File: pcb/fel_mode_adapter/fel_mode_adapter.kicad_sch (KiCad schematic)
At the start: 4 parts, among them J1 USB_A, P1 USB_C_Plug_USB2.0

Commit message: Fix the board: add a regulator and farnelle references. Add a pull up on boot0
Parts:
- J1: farnell (none) -> 2313729
- P1: farnell (none) -> 3777659
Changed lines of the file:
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@@
+			)
+		)
+		(property "farnell" "2313729"
+			(at 175.26 85.09 0)
+			(effects
+				(font
+					(size 1.27 1.27)
+				)
+				(hide yes)
 			)
 		)
@@
 			(at 109.22 87.63 0)
 			(effects
+				(font
+					(size 1.27 1.27)
+				)
+				(hide yes)
+			)
+		)
+		(property "farnell" "3777659"
+			(at 109.22 87.63 0)
+			(effects

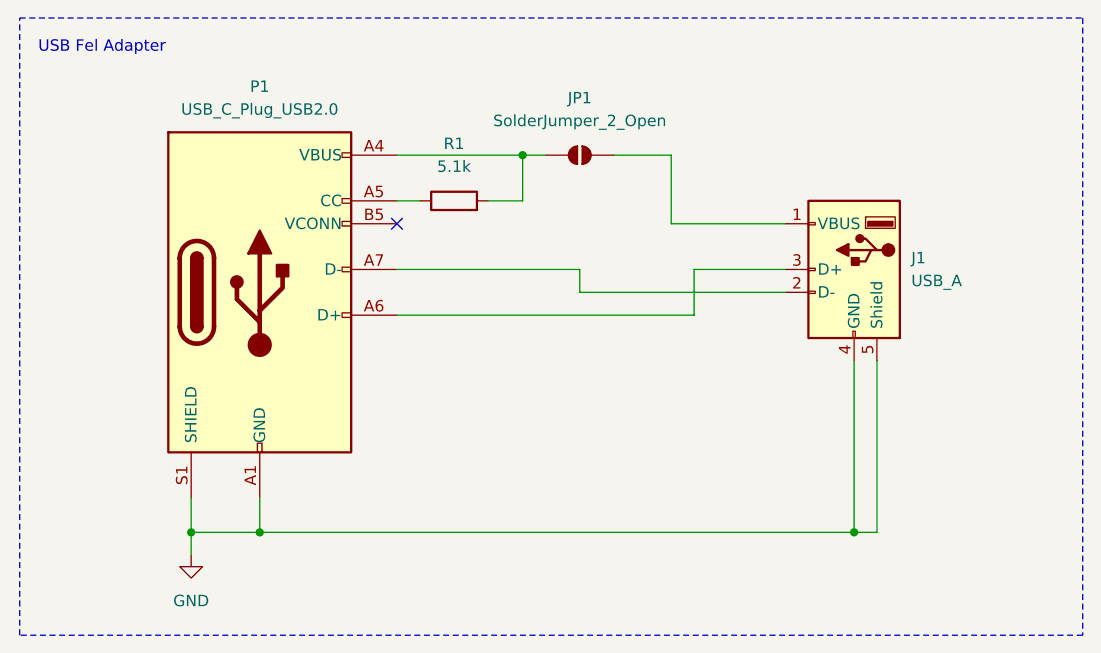
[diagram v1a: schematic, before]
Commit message: Adds a GND test point to the FEL mode adapter.
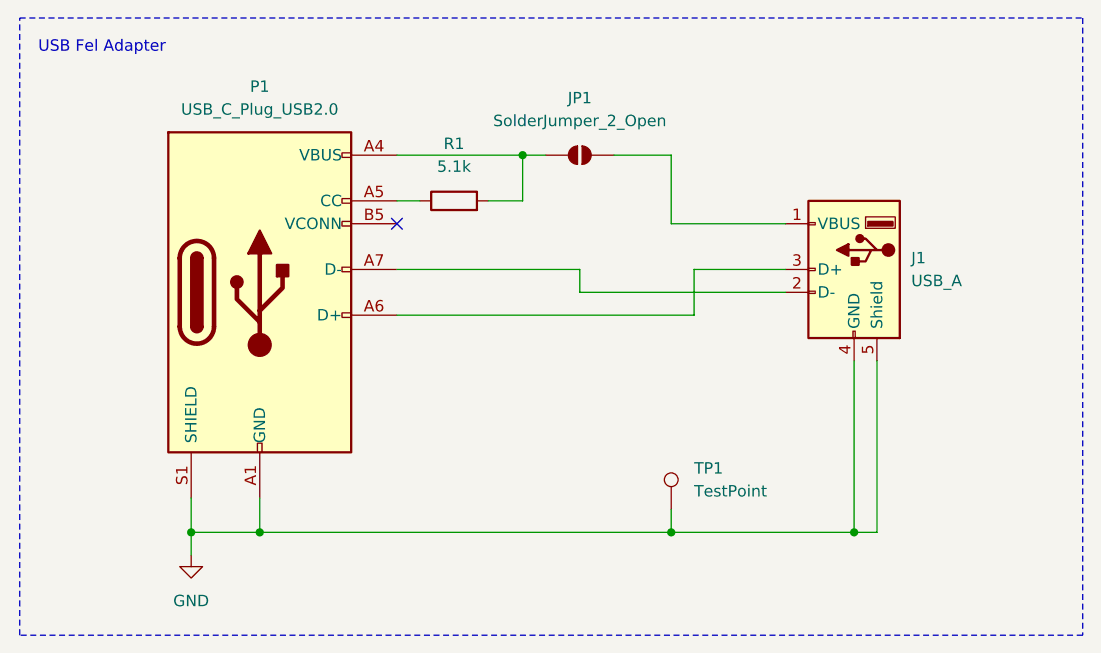
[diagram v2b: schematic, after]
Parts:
- added TP1: TestPoint, TestPoint:TestPoint_Pad_D1.0mm, symbol Connector:TestPoint
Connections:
- net GND: now also TP1.1
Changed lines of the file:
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@@
+		(color 0 0 0 0)
+	)
+	(junction
+		(at 154.94 114.3)
+		(diameter 0)
 		(color 0 0 0 0)
 	)
@@
 	(wire
 		(pts
+			(xy 154.94 114.3) (xy 109.22 114.3)
+		)
+		(stroke
+			(width 0)
+			(type default)
+		)
+	)
+	(wire
+		(pts
 			(xy 124.46 90.17) (xy 157.48 90.17)
 		)
@@
 	(wire
 		(pts
+			(xy 154.94 111.76) (xy 154.94 114.3)
+		)
+		(stroke
+			(width 0)
+			(type default)
+		)
+	)
+	(wire
+		(pts
 			(xy 177.8 114.3) (xy 175.26 114.3)
 		)
@@
 	(wire
 		(pts
-			(xy 175.26 114.3) (xy 109.22 114.3)
+			(xy 175.26 114.3) (xy 154.94 114.3)
 		)
 		(stroke
@@
 					(unit 1)
 				)
+			)
+		)
+	)
+	(symbol
+		(lib_id "Connector:TestPoint")
+		(at 154.94 111.76 0)
+		(unit 1)
+		(exclude_from_sim no)
+		(in_bom yes)
+		(on_board yes)
+		(dnp no)
+		(fields_autoplaced yes)
+		(property "Reference" "TP1"
+			(at 157.48 107.1879 0)
+			(effects
+				(font
+					(size 1.27 1.27)
+				)
+				(justify left)
+			)
+		)
+		(property "Value" "TestPoint"
+			(at 157.48 109.7279 0)
+			(effects
+				(font
+					(size 1.27 1.27)
+				)
+				(justify left)
+			)
+		)
+		(property "Footprint" "TestPoint:TestPoint_Pad_D1.0mm"
+			(at 160.02 111.76 0)
+			(effects
+				(font
+					(size 1.27 1.27)
+				)
+				(hide yes)
+			)
+		)
+		(property "Datasheet" "~"
+			(at 160.02 111.76 0)
+			(effects
+				(font
+					(size 1.27 1.27)
+				)
+				(hide yes)
+			)
+		)
+		(property "Description" "test point"
+			(at 154.94 111.76 0)
+			(effects
+				(font
+					(size 1.27 1.27)
+				)
+				(hide yes)
+			)
+		)
+		(pin "1"
+		)
+		(instances
+			(project ""
+				(path "/1418d05e-d255-4e21-84d2-420121b241e4"
+					(reference "TP1")
+					(unit 1)
+				)

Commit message: Updating the uart and fel mode adapter after soldering it.
Manufacturing shiwed the pcb to be too large and the gnd wire connector
too close to the uart connector. The farnell reference resistor on the
fel mode adapter was of the wrong foorprint.
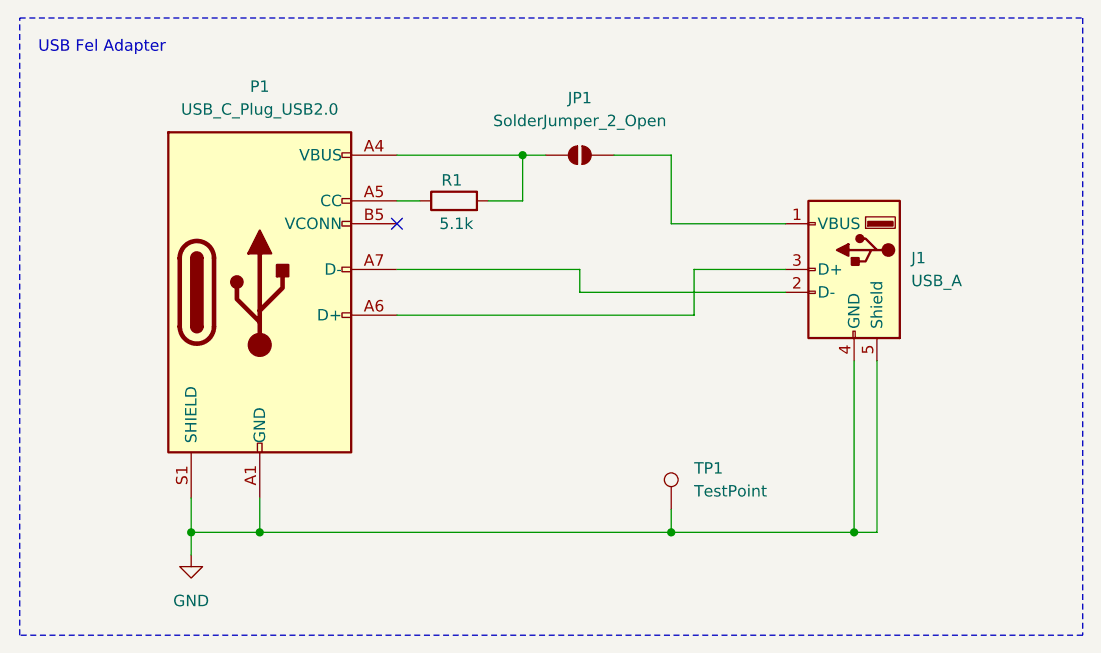
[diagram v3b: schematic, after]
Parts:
- R1: farnell (none) -> 9334645
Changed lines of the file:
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@@
 		(on_board yes)
 		(dnp no)
-		(fields_autoplaced yes)
 		(property "Reference" "R1"
-			(at 130.81 71.12 90)
+			(at 130.556 75.184 90)
 			(effects
 				(font
@@
 		)
 		(property "Value" "5.1k"
-			(at 130.81 73.66 90)
+			(at 131.064 80.01 90)
 			(effects
 				(font
@@
 			(at 130.81 77.47 0)
 			(effects
+				(font
+					(size 1.27 1.27)
+				)
+				(hide yes)
+			)
+		)
+		(property "farnell" "9334645"
+			(at 130.81 77.47 0)
+			(effects
